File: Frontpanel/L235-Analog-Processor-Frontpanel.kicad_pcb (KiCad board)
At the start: 2 copper layers, 60 x 128.5 mm, 0 parts

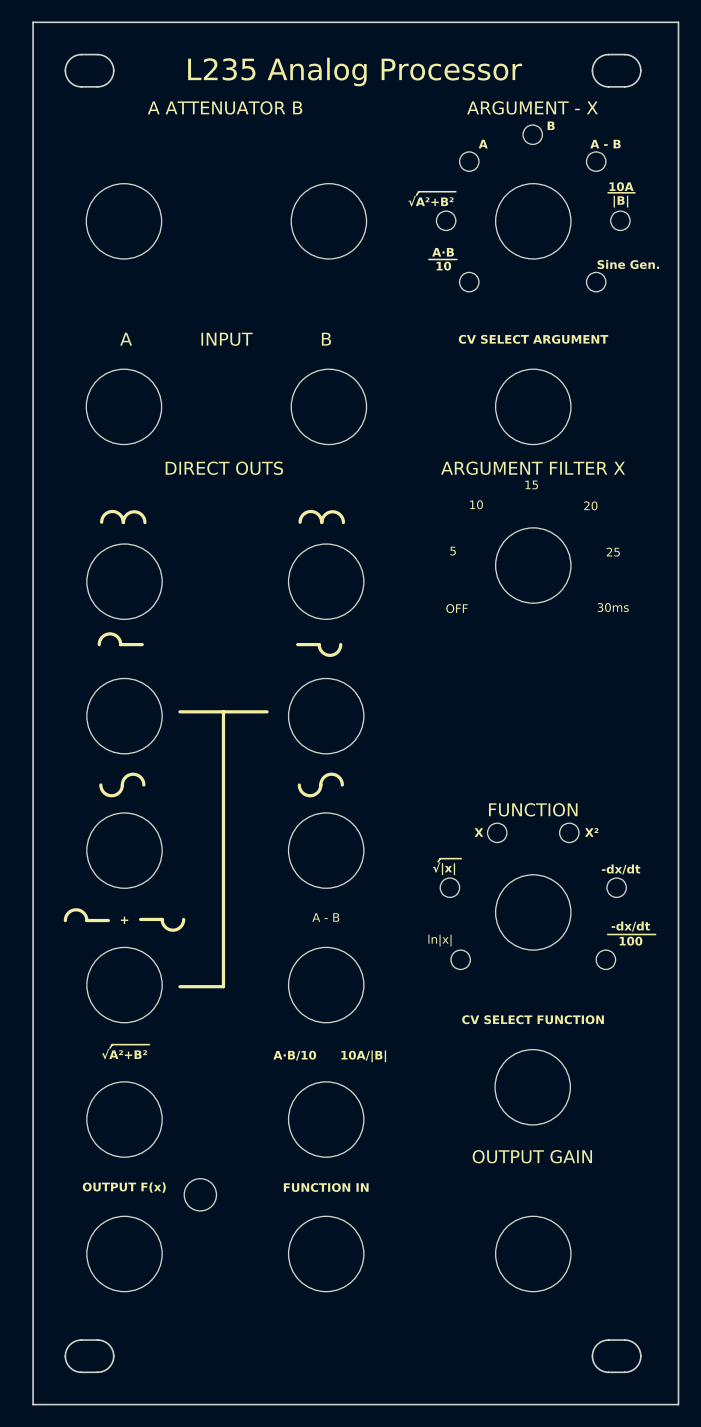
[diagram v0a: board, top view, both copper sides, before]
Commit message: Updated frontpanel with Bias knobs, removing invert outs
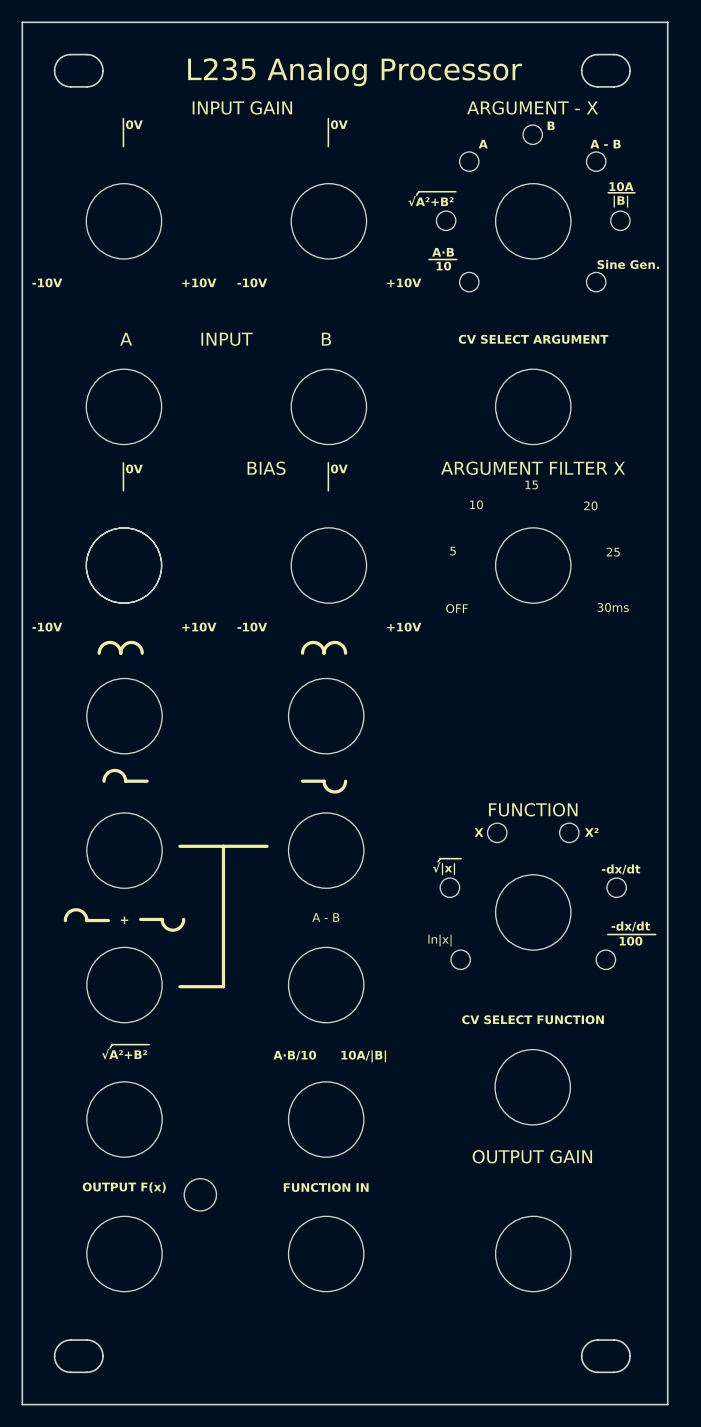
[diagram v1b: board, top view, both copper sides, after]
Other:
- outline, holes or cut-outs redrawn
- board text added: "+10V"
- board text added: "-10V"
- board text added: "0V"
- board text added: "BIAS"
- board text added: "INPUT GAIN"
- board text removed: "A ATTENUATOR B"
- board text removed: "DIRECT OUTS"

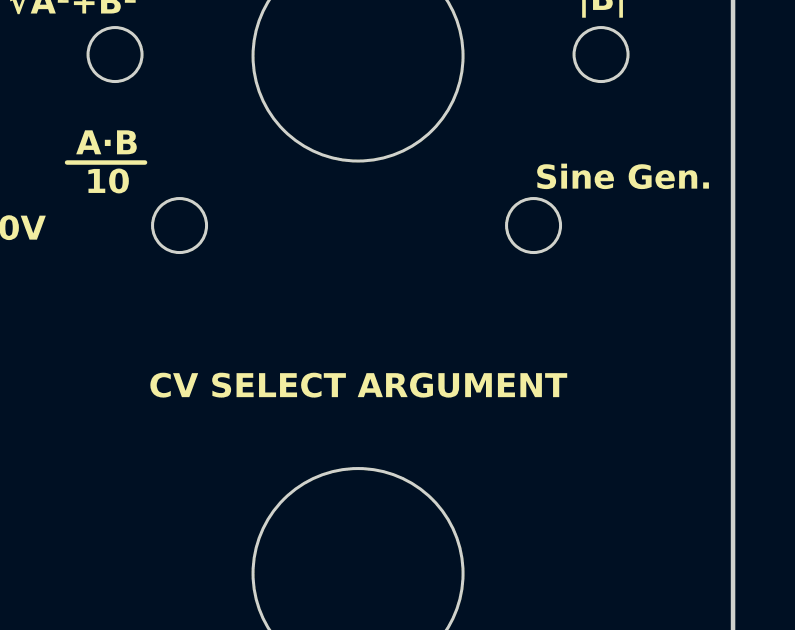
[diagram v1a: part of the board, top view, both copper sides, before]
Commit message: Fixed attenuverter circuit after breadboard testing
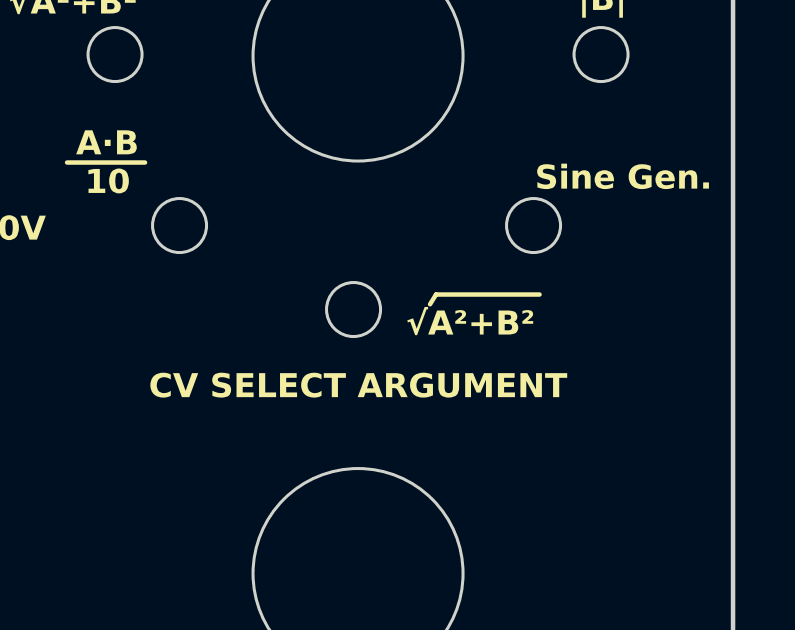
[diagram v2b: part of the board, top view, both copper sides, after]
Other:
- outline, holes or cut-outs redrawn
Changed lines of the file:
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@@
   (gr_arc (start 74.75 103.15) (mid 73.75 104.15) (end 72.75 103.15)
     (stroke (width 0.3) (type default)) (layer "F.SilkS"))
+  (gr_line (start 109.85 46.2) (end 109.65 46.525)
+    (stroke (width 0.15) (type default)) (layer "F.SilkS"))
   (gr_line (start 72.75 103.15) (end 70.75 103.15)
     (stroke (width 0.3) (type default)) (layer "F.SilkS"))
+  (gr_line (start 109.85 46.2) (end 113.3 46.2)
+    (stroke (width 0.15) (type default)) (layer "F.SilkS"))
   (gr_arc (start 68.9 78.4) (mid 69.9 77.4) (end 70.9 78.4)
     (stroke (width 0.3) (type default)) (layer "F.SilkS"))
@@
     (stroke (width 0.1) (type default)) (fill none) (layer "Edge.Cuts"))
   (gr_circle (center 69.2 55.5) (end 72.7 55.5)
+    (stroke (width 0.1) (type default)) (fill none) (layer "Edge.Cuts"))
+  (gr_circle (center 107.1 46.7) (end 108 46.7)
     (stroke (width 0.1) (type default)) (fill none) (layer "Edge.Cuts"))
   (gr_arc (start 111.75 143.75) (mid 112.18934 142.68934) (end 113.25 142.25)
@@
     (effects (font (size 0.8 0.8) (thickness 0.15)) (justify left bottom))
   )
+  (gr_text "√A²+B²" (at 111 47.1625) (layer "F.SilkS")
+    (effects (font (size 0.8 0.8) (thickness 0.15) bold))
+  )
   (gr_text "A            INPUT            B" (at 78.7 49.25) (layer "F.SilkS")
